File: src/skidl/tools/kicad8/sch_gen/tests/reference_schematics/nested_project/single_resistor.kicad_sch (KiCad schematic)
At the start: 1 part

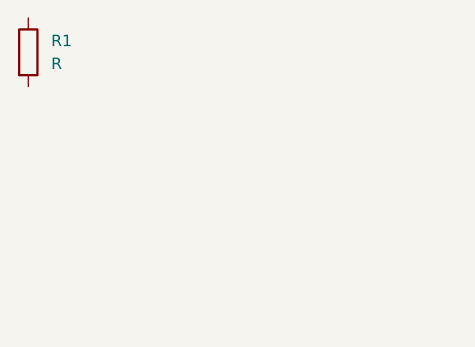
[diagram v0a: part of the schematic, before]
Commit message: add footprint and value to resistors
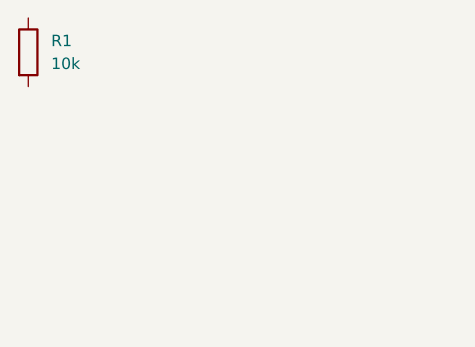
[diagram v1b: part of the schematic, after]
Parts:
- R1: value R -> 10k; footprint (none) -> Resistor_SMD:R_0603_1608Metric
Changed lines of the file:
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@@
 			)
 		)
-		(property "Value" "R"
+		(property "Value" "10k"
 			(at 2.54 1.2699 0)
 			(effects
@@
 			)
 		)
-		(property "Footprint" ""
+		(property "Footprint" "Resistor_SMD:R_0603_1608Metric"
 			(at -1.778 0 90)
 			(effects
